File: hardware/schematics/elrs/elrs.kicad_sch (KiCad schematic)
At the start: 47 parts, among them U13 SX1281IMLTRT, U14 ESP32-C3, U15 TLV75533PDQNR, X2 CJ17-400001010B20

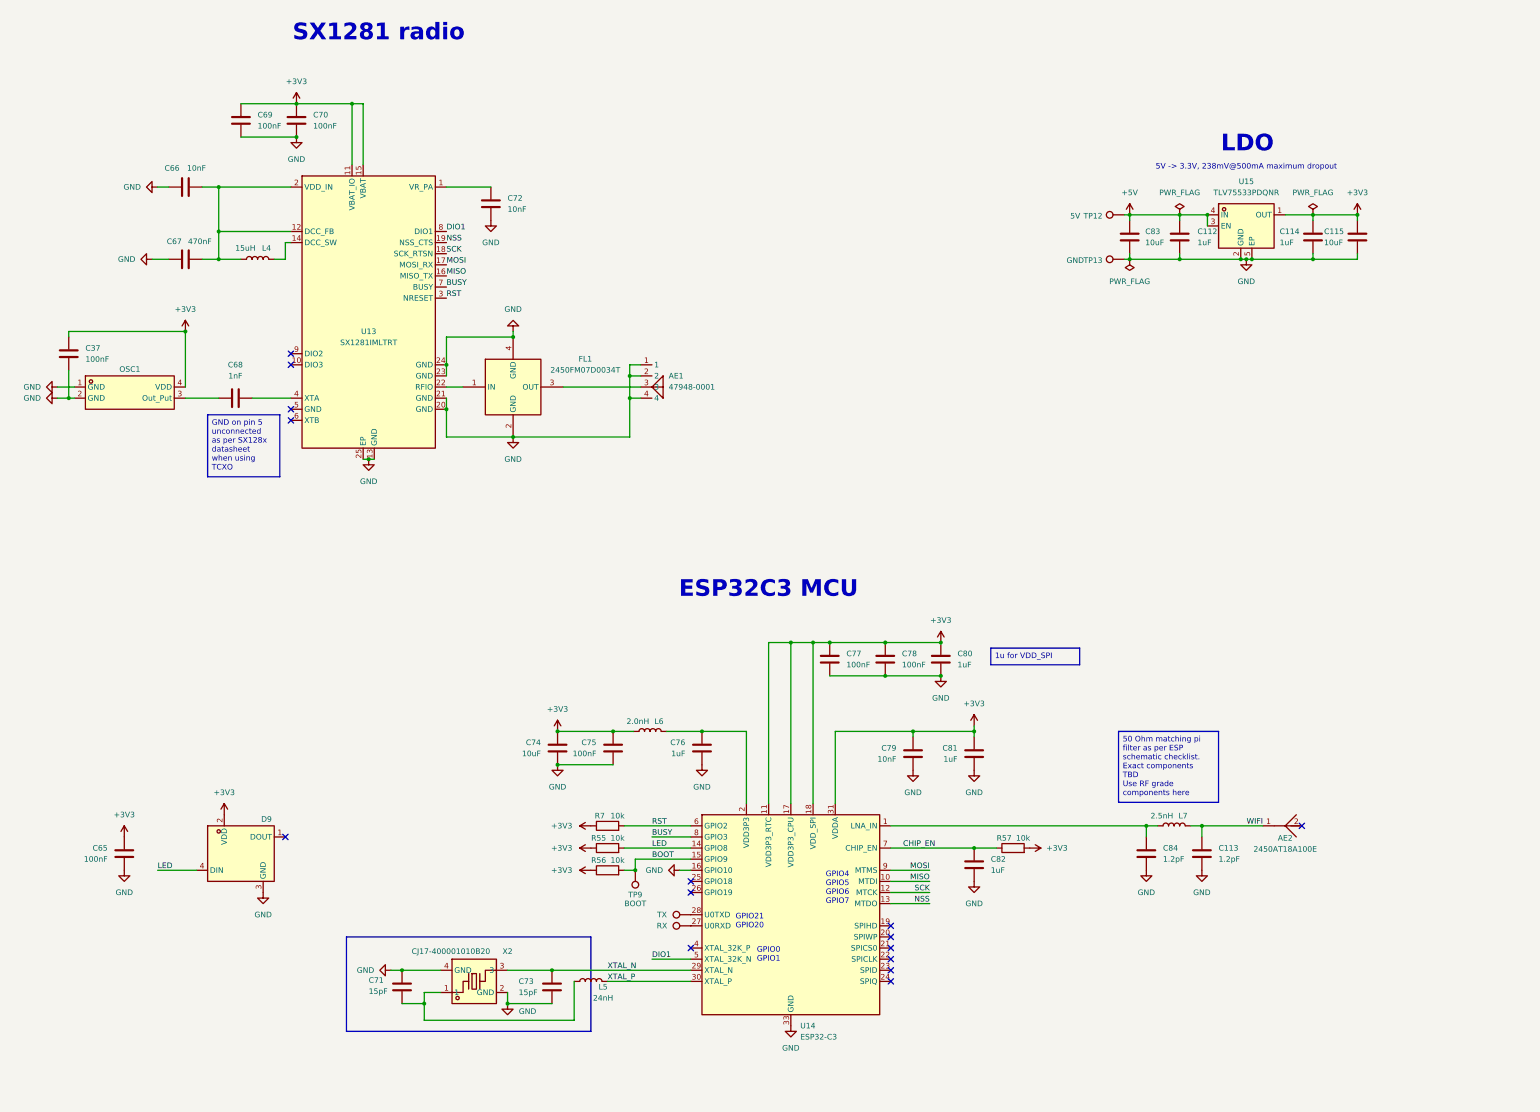
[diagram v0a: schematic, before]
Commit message: Whoop setup: restructure, import current FC/RX sheets, Bluejay libs, research docs
- KiCad project moved under hardware/ (family convention)
- FC sheets <- OpenFC-Lite-Mini rev2 (osd dropped: digital-only, root never
  referenced it); ELRS sheet <- OpenRX-Lite; orphaned esc_main deleted;
  esc_channel x4 kept as inherited placeholder pending Bluejay redraw
- Libraries replaced: lib (Lite-Mini), components/4in1ESC (4in1-mini donors),
  OpenRX-Shared (3D paths rewritten project-local via pcbnew API), new 'whoop'
  lib re-imported fresh via easyeda2kicad (EFM8BB51F16G, AGM310MAP, BY25Q64)
- sym-lib-table duplicate stale iCloud OpenRX-Shared entries fixed
- datasheets/ assembled (FC/ESC/ELRS); stale toothpick ESC docs removed
- docs/ESC_DESIGN.md extended with 2026-06 sourcing + market reality check
  (AGM310MAP thermal/supply limits, 12A class floor, BY25Q64 substitute)
- README/market research rewritten for digital-only Bluejay whoop scope
- Hierarchy verified via kicad-cli netlist export

Co-Authored-By: Claude Fable 5 <noreply@anthropic.com>
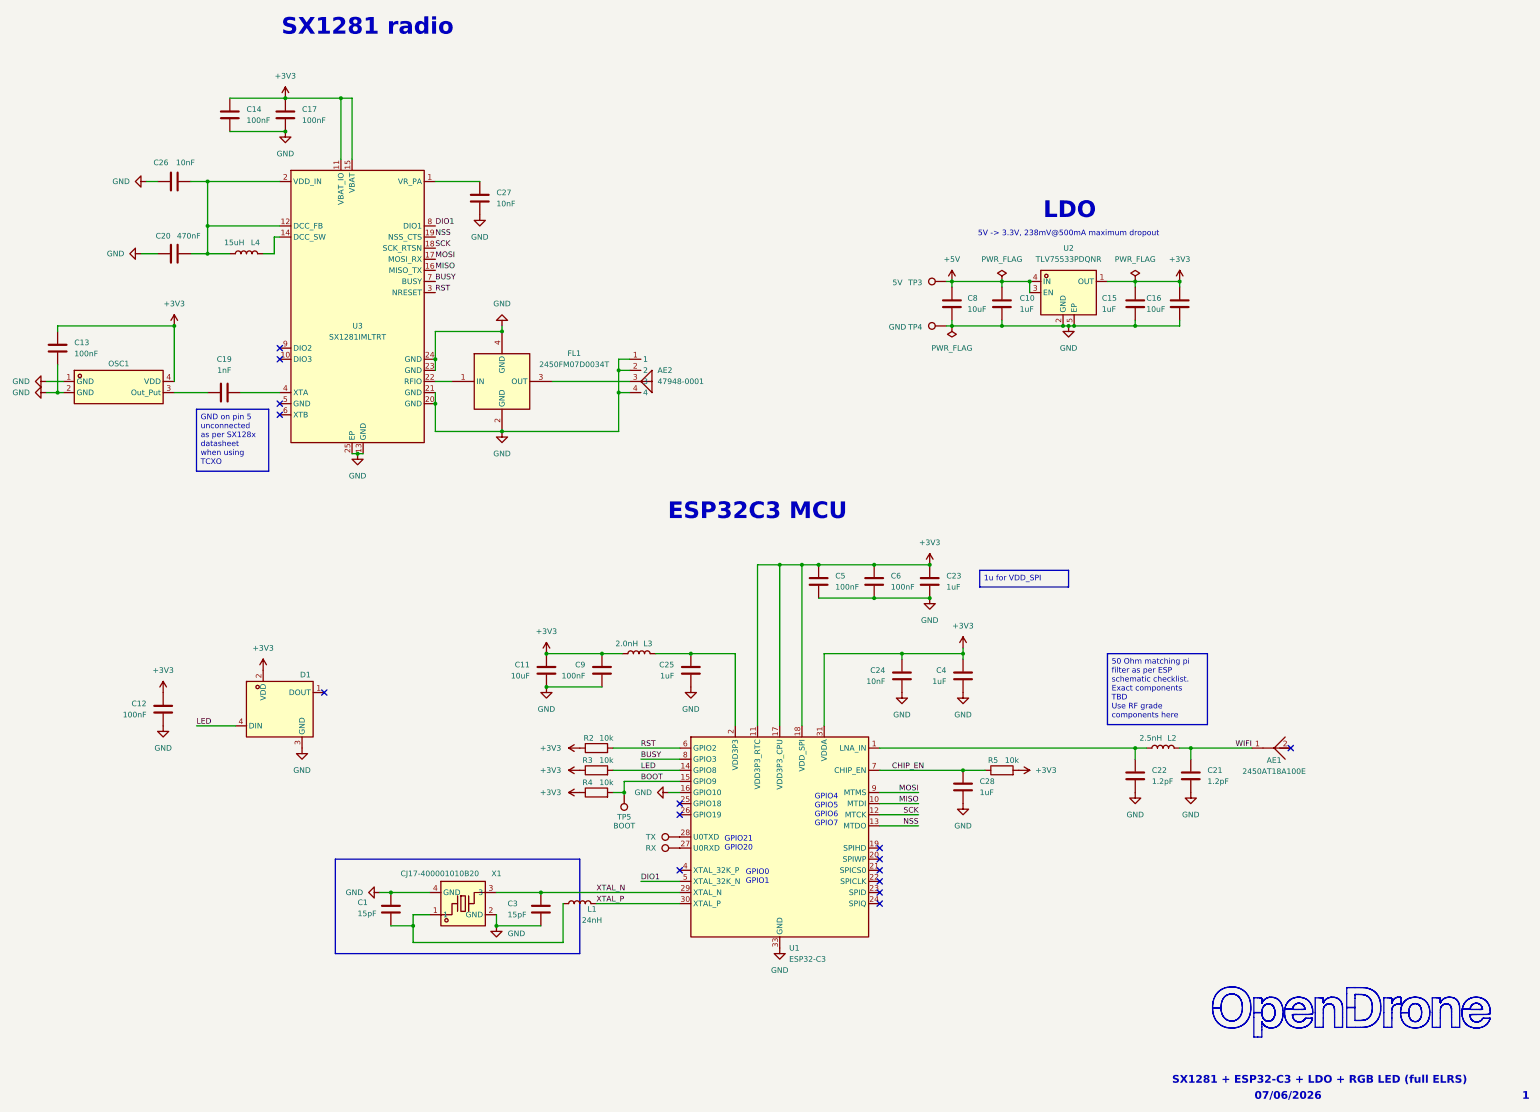
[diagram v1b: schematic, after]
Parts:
- renumbered AE2 to AE1, AE1 to AE2, C71 to C1, C112 to C10, C74 to C11, C65 to C12, C37 to C13, C69 to C14, C114 to C15, C115 to C16, C70 to C17, C68 to C19, C67 to C20, C113 to C21, C84 to C22, C80 to C23, C79 to C24, C76 to C25, C66 to C26, C72 to C27, C82 to C28, C73 to C3, C81 to C4, C77 to C5, C78 to C6, C83 to C8, C75 to C9, D9 to D1, L5 to L1, L7 to L2, L6 to L3, R7 to R2, R55 to R3, R56 to R4, R57 to R5, TP11 to TP1, TP10 to TP2, TP12 to TP3, TP13 to TP4, TP9 to TP5, U14 to U1, U15 to U2, U13 to U3, X2 to X1
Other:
- note added: "07/06/2026"
- note added: "1"
- note added: "SX1281 + ESP32-C3 + LDO + RGB LED (full ELRS)"
- moved on the sheet: AE1, AE2, C1, C10, C11, C12, C13, C14, C15, C16, C17, C19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
